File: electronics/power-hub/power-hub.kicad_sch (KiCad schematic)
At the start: 0 parts

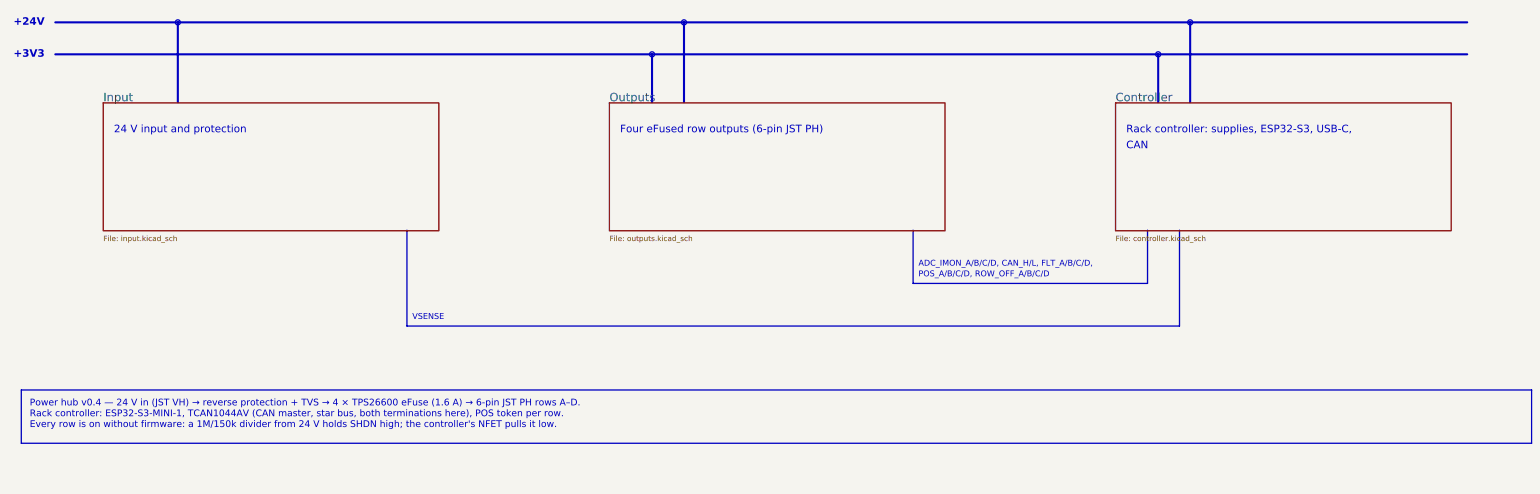
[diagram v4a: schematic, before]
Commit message: Power hub v0.5: USB-C PD input (AP33772S), 4 layers, rows off until enabled
The rack now runs from one USB PD 3.1 charger instead of the GST60A24 brick.

Hub v0.5 (76 x 140 mm, 4 layers, In1 GND, In2 VRACK/+3V3):
* AP33772S sink: 20 V at power-up (VSEL 39k), 28 V EPR on the controller's
  request, never 36/48 V; 5 mOhm Kelvin shunt, back-to-back IRF7842 switch,
  SMAJ30A TVS, NTC by the switch, interrupt and I2C to the ESP32-S3.
* USB4105 5 A receptacle; the controller's buck runs from VBUS (5-28 V),
  ahead of the switch.
* Every row's TPS26600 is off until the controller drives ROW_EN (SHDN pulled
  low); IMON per row; front PD LED.
* ERC 0, DRC 0 errors, 0 unconnected, parity 0; 146 3D models, 0 stand-ins.

Power box: 84 x 148 x 35 mm, hub only (no brick, no cradles), rear USB-C
cut-out, lid on corner lugs.  Viewer, BOM (charger + 5 A e-marked cable,
4-layer JLC estimate) and docs (power, mechanical, cabling, assembly,
electronics) follow.

Co-Authored-By: Claude Opus 5.5 <noreply@anthropic.com>
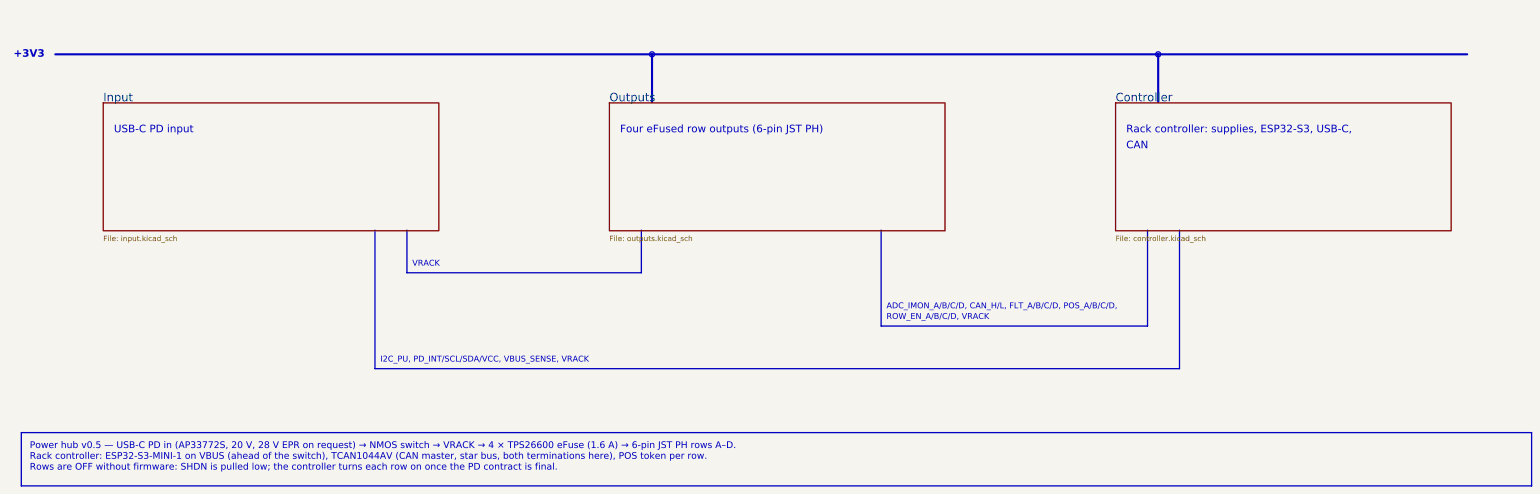
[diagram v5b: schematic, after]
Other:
- note added: "ADC_IMON_A/B/C/D, CAN_H/L, FLT_A/B/C/D, POS_A/B/C/D,"
- note added: "I2C_PU, PD_INT/SCL/SDA/VCC, VBUS_SENSE, VRACK"
- note added: "ROW_EN_A/B/C/D, VRACK"
- note added: "USB-C PD input"
- note added: "VRACK"
- note removed: "+24V"
- note removed: "24 V input and protection"
- note removed: "ADC_IMON_A/B/C/D, CAN_H/L, FLT_A/B/C/D,"
- note removed: "POS_A/B/C/D, ROW_OFF_A/B/C/D"
- note removed: "VSENSE"
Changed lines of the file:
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@@
 	(title_block
 		(title "Power hub — Overview")
-		(rev "0.4")
+		(rev "0.5")
 		(company "hw-testing-rack")
-		(comment 1 "24 V distribution + rack controller (ESP32-S3, CAN master) for the hw-testing-rack")
+		(comment 1 "USB-C PD distribution + rack controller (ESP32-S3, CAN master) for the hw-testing-rack")
 		(comment 2 "Generated from electronics/power-hub/design.py — edit the Python, then regenerate")
 	)
@@
 		)
 	)
-	(text "24 V input and protection"
+	(text "USB-C PD input"
 		(exclude_from_sim no)
 		(at 52.07 77.47 0)
@@
 	(polyline
 		(pts
-			(xy 38.1 50.8)
-			(xy 374.65 50.8)
-		)
-		(stroke
-			(width 0.5)
-			(type default)
-		)
-		(fill
-			(type none)
-		)
-	)
-	(text "+24V"
-		(exclude_from_sim no)
-		(at 35.56 50.8 0)
-		(effects
-			(font
-				(size 1.8 1.8)
-				(bold yes)
-			)
-			(justify right)
-		)
-	)
-	(polyline
-		(pts
-			(xy 67.31 50.8)
-			(xy 67.31 69.85)
-		)
-		(stroke
-			(width 0.5)
-			(type default)
-		)
-		(fill
-			(type none)
-		)
-	)
-	(circle
-		(center 67.31 50.8)
-		(radius 0.6)
-		(stroke
-			(width 0.3)
-			(type default)
-		)
-		(fill
-			(type outline)
-		)
-	)
-	(polyline
-		(pts
-			(xy 187.96 50.8)
-			(xy 187.96 69.85)
-		)
-		(stroke
-			(width 0.5)
-			(type default)
-		)
-		(fill
-			(type none)
-		)
-	)
-	(circle
-		(center 187.96 50.8)
-		(radius 0.6)
-		(stroke
-			(width 0.3)
-			(type default)
-		)
-		(fill
-			(type outline)
-		)
-	)
-	(polyline
-		(pts
-			(xy 308.61 50.8)
-			(xy 308.61 69.85)
-		)
-		(stroke
-			(width 0.5)
-			(type default)
-		)
-		(fill
-			(type none)
-		)
-	)
-	(circle
-		(center 308.61 50.8)
-		(radius 0.6)
-		(stroke
-			(width 0.3)
-			(type default)
-		)
-		(fill
-			(type outline)
-		)
-	)
-	(polyline
-		(pts
-			(xy 242.57 100.33)
-			(xy 242.57 113.03)
-			(xy 298.45 113.03)
+			(xy 121.92 100.33)
+			(xy 121.92 110.49)
+			(xy 177.8 110.49)
+			(xy 177.8 100.33)
+		)
+		(stroke
+			(width 0.3)
+			(type default)
+		)
+		(fill
+			(type none)
+		)
+	)
+	(text "VRACK"
+		(exclude_from_sim no)
+		(at 123.19 109.22 0)
+		(effects
+			(font
+				(size 1.4 1.4)
+			)
+			(justify left bottom)
+		)
+	)
+	(polyline
+		(pts
+			(xy 234.95 100.33)
+			(xy 234.95 123.19)
+			(xy 298.45 123.19)
 			(xy 298.45 100.33)
 		)
@@
 		)
 	)
-	(text "ADC_IMON_A/B/C/D, CAN_H/L, FLT_A/B/C/D,"
-		(exclude_from_sim no)
-		(at 243.84 109.22 0)
+	(text "ADC_IMON_A/B/C/D, CAN_H/L, FLT_A/B/C/D, POS_A/B/C/D,"
+		(exclude_from_sim no)
+		(at 236.22 119.38 0)
 		(effects
 			(font
@@
 		)
 	)
-	(text "POS_A/B/C/D, ROW_OFF_A/B/C/D"
-		(exclude_from_sim no)
-		(at 243.84 111.76 0)
+	(text "ROW_EN_A/B/C/D, VRACK"
+		(exclude_from_sim no)
+		(at 236.22 121.92 0)
 		(effects
 			(font
@@
 	(polyline
 		(pts
-			(xy 121.92 100.33)
-			(xy 121.92 123.19)
-			(xy 306.07 123.19)
+			(xy 114.3 100.33)
+			(xy 114.3 133.35)
+			(xy 306.07 133.35)
 			(xy 306.07 100.33)
 		)
@@
 		)
 	)
-	(text "VSENSE"
-		(exclude_from_sim no)
-		(at 123.19 121.92 0)
+	(text "I2C_PU, PD_INT/SCL/SDA/VCC, VBUS_SENSE, VRACK"
+		(exclude_from_sim no)
+		(at 115.57 132.08 0)
 		(effects
 			(font
@@
 		)
 	)
-	(text_box "Power hub v0.4 — 24 V in (JST VH) → reverse protection + TVS → 4 × TPS26600 eFuse (1.6 A) → 6-pin JST PH rows A–D.\nRack controller: ESP32-S3-MINI-1, TCAN1044AV (CAN master, star bus, both terminations here), POS token per row.\nEvery row is on without firmware: a 1M/150k divider from 24 V holds SHDN high; the controller's NFET pulls it low."
-		(exclude_from_sim no)
-		(at 30 138.43 0)
+	(text_box "Power hub v0.5 — USB-C PD in (AP33772S, 20 V, 28 V EPR on request) → NMOS switch → VRACK → 4 × TPS26600 eFuse (1.6 A) → 6-pin JST PH rows A–D.\nRack controller: ESP32-S3-MINI-1 on VBUS (ahead of the switch), TCAN1044AV (CAN master, star bus, both terminations here), POS token per row.\nRows are OFF without firmware: SHDN is pulled low; the controller turns each row on once the PD contract is final."
+		(exclude_from_sim no)
+		(at 30 148.59 0)
 		(size 360 12.7)
 		(margins 2 2 2 2)

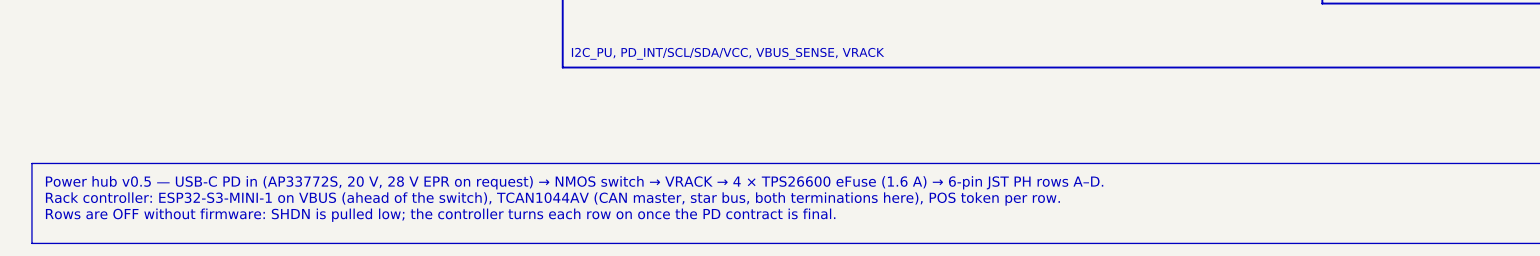
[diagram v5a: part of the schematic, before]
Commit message: CAN transceiver: TCAN1462V (signal improvement) on the hub and the bay node
Same SOIC-8 pinout as the TCAN1044AV (VIO on pin 5, STB on pin 8), so the
footprint, placement and routing are unchanged: the regenerated PCBs keep
every track and via, only U6 / U11's value and fields change.  Signal
improvement (CiA 601-4, ISO 11898-2:2024 set C) damps the ringing of the
star's open branch ends; the termination (56 ohm at the hub) stays.

* catalog: TCAN1462VDRQ1 (C7399456, no LCSC stock on 2026-10-18), with the
  TCAN1044AVDRQ1 (C3234993) and NXP TJA1462AT/0Z (C3234095) as alternates;
  CPL rotation for all three.
* BOM: the board BOMs' alternates now show in the rack BOM notes; JLC
  estimates +$0.54 per board.
* docs/can.md: why the star is fine at 250 kbit/s and what SIC adds, with
  sources (TI SLLSFF2B, SLLA581A; CiA bit-timing table; NXP TJA1462).
* Both boards: ERC 0, DRC 0 errors, 0 unconnected, parity 0; 3D 0 stand-ins.

Co-Authored-By: Claude Opus 5.5 <noreply@anthropic.com>
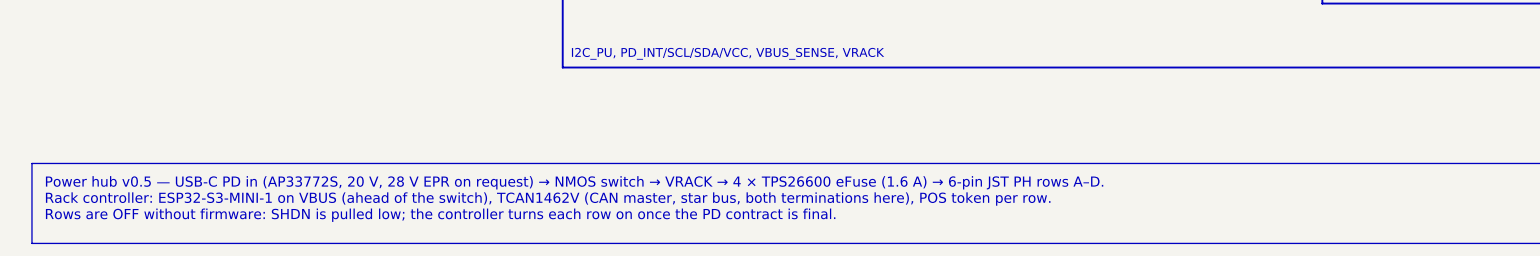
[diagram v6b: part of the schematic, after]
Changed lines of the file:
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@@
 		)
 	)
-	(text_box "Power hub v0.5 — USB-C PD in (AP33772S, 20 V, 28 V EPR on request) → NMOS switch → VRACK → 4 × TPS26600 eFuse (1.6 A) → 6-pin JST PH rows A–D.\nRack controller: ESP32-S3-MINI-1 on VBUS (ahead of the switch), TCAN1044AV (CAN master, star bus, both terminations here), POS token per row.\nRows are OFF without firmware: SHDN is pulled low; the controller turns each row on once the PD contract is final."
+	(text_box "Power hub v0.5 — USB-C PD in (AP33772S, 20 V, 28 V EPR on request) → NMOS switch → VRACK → 4 × TPS26600 eFuse (1.6 A) → 6-pin JST PH rows A–D.\nRack controller: ESP32-S3-MINI-1 on VBUS (ahead of the switch), TCAN1462V (CAN master, star bus, both terminations here), POS token per row.\nRows are OFF without firmware: SHDN is pulled low; the controller turns each row on once the PD contract is final."
 		(exclude_from_sim no)
 		(at 30 148.59 0)

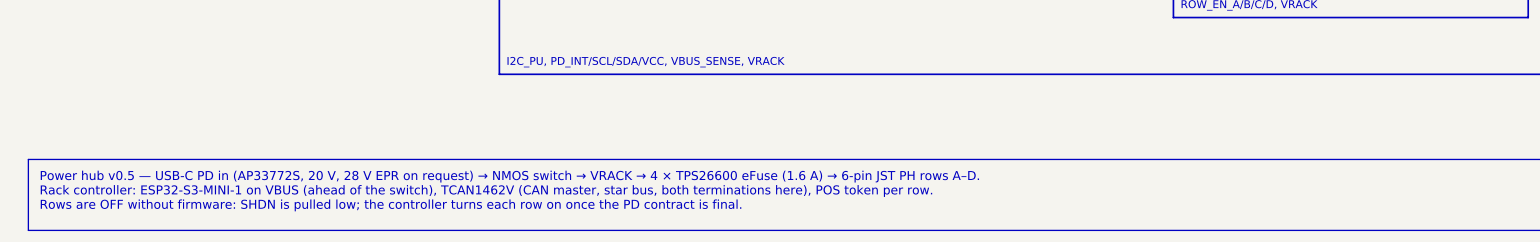
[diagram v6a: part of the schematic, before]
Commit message: Power hub: U1 is the AP33772S FA01 (5 V first), bought through JLC Global Sourcing
The FA02 (VSEL: 20 V by itself) is out of stock everywhere until
≈ 14/12/2026; the user approved the FA01 (2026-10-19): same die, package,
pinout and I2C map, pins 7 and 11 NC.  It takes the charger's 5 V first;
the firmware (7b8a705) sets VSELMIN to 15 V and asks for 20 V / 28 V EPR,
and the rows stay locked out below 15 V.  R7 (an FA02's VSEL resistor)
stays fitted, so an FA02 drops in later.

- catalog: AP33772SDKZ-13-FA01, LCSC C24374260 (0 stock), DigiKey via
  JLC Global Sourcing.
- Hub schematic notes and BOMs regenerated; the routing is the same
  session re-imported (1241 segments, 583 vias, as on main).  ERC 0,
  DRC 0 errors / 0 unconnected / parity 0 (one silk warning, as on main).
- bom.py hub estimate ≈ $227: + $13.30 for 5 parts through Global
  Sourcing (JLC's markup reported ≈ 50 %, no official figure) and
  ≈ 2 weeks for them to reach JLC.
- docs/power.md step 1 and sourcing, electronics.md hub rows,
  bom/sourcing.md: the choice.

Co-Authored-By: Claude Opus 5.5 <noreply@anthropic.com>
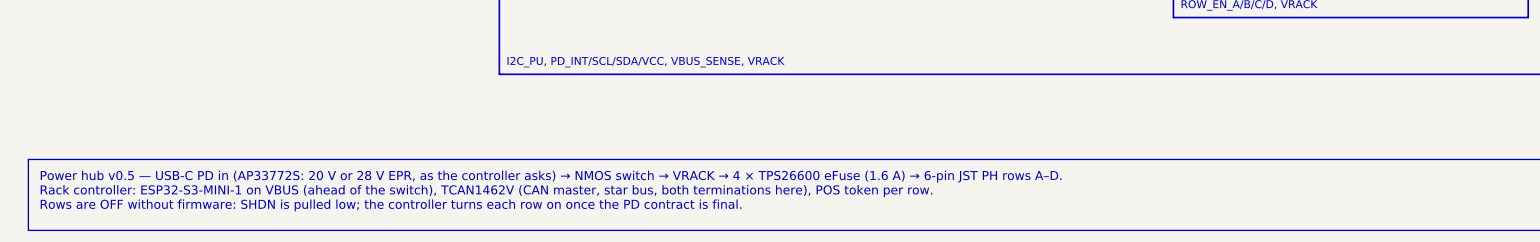
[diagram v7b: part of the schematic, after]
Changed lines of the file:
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@@
 		)
 	)
-	(text_box "Power hub v0.5 — USB-C PD in (AP33772S, 20 V, 28 V EPR on request) → NMOS switch → VRACK → 4 × TPS26600 eFuse (1.6 A) → 6-pin JST PH rows A–D.\nRack controller: ESP32-S3-MINI-1 on VBUS (ahead of the switch), TCAN1462V (CAN master, star bus, both terminations here), POS token per row.\nRows are OFF without firmware: SHDN is pulled low; the controller turns each row on once the PD contract is final."
+	(text_box "Power hub v0.5 — USB-C PD in (AP33772S: 20 V or 28 V EPR, as the controller asks) → NMOS switch → VRACK → 4 × TPS26600 eFuse (1.6 A) → 6-pin JST PH rows A–D.\nRack controller: ESP32-S3-MINI-1 on VBUS (ahead of the switch), TCAN1462V (CAN master, star bus, both terminations here), POS token per row.\nRows are OFF without firmware: SHDN is pulled low; the controller turns each row on once the PD contract is final."
 		(exclude_from_sim no)
 		(at 30 148.59 0)

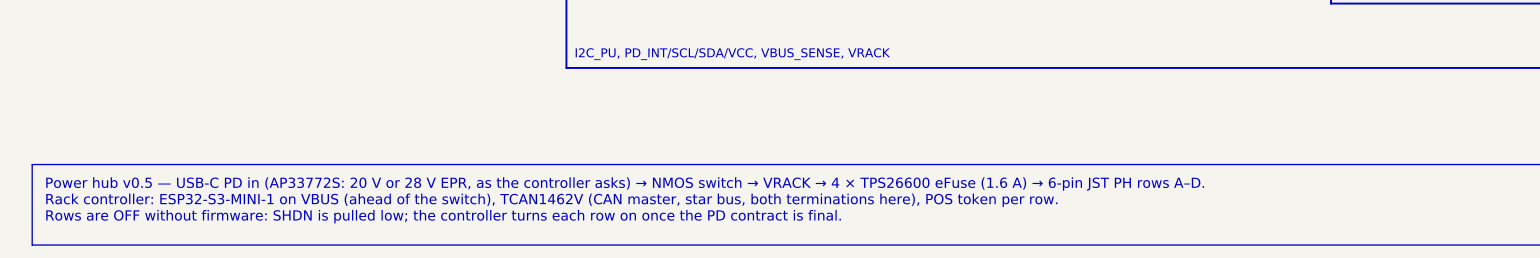
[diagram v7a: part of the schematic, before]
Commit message: CAN transceiver: the TJA1462AT on the hub and the node
The TCAN1462V (C7399456) had no LCSC stock on 2026-10-18 and 19, and
JLC's quote of the hub asked for another part.  The user chose NXP's
TJA1462AT/0Z (C3234095, 10 500 in stock) for both boards (hub U6, node
U11): the same SOIC-8 pinout (VIO on pin 5, STB on pin 8), signal
improvement kept, bus pins -36/+40 V instead of ±58 V.  The TCAN1462V
and the TCAN1044AV stay the alternates.

Both boards regenerated and the same Freerouting sessions re-imported
(tracks and vias unchanged): ERC 0, DRC 0 errors (the hub's known C8
silkscreen warning), 0 unconnected, parity 0, JLC READY.  The CPL keeps
its 270° correction (C3234095 was already in build_board.py).

Docs: can.md, electronics.md, firmware comments and pin tables,
bom/sourcing.md, which also notes that JLC unticks the USB4105 (hard to
process, $0.03 a piece): tick it again at every order.

Co-Authored-By: Claude Opus 5.5 <noreply@anthropic.com>
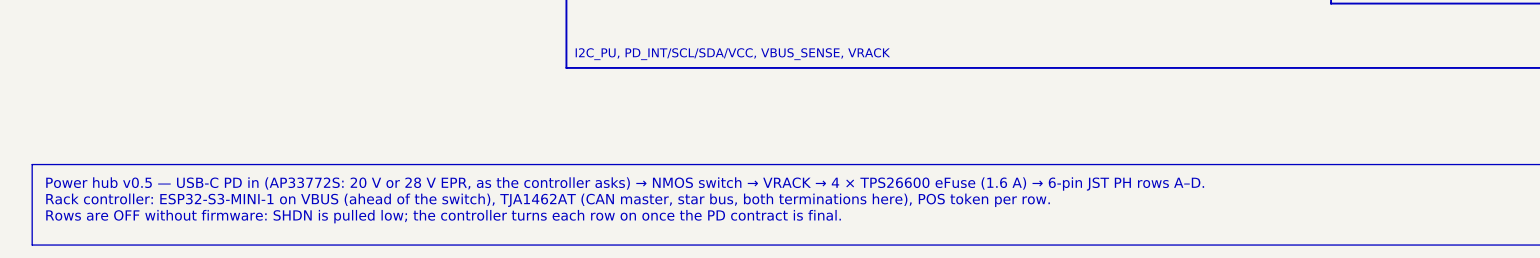
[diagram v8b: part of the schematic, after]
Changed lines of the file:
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@@
 		)
 	)
-	(text_box "Power hub v0.5 — USB-C PD in (AP33772S: 20 V or 28 V EPR, as the controller asks) → NMOS switch → VRACK → 4 × TPS26600 eFuse (1.6 A) → 6-pin JST PH rows A–D.\nRack controller: ESP32-S3-MINI-1 on VBUS (ahead of the switch), TCAN1462V (CAN master, star bus, both terminations here), POS token per row.\nRows are OFF without firmware: SHDN is pulled low; the controller turns each row on once the PD contract is final."
+	(text_box "Power hub v0.5 — USB-C PD in (AP33772S: 20 V or 28 V EPR, as the controller asks) → NMOS switch → VRACK → 4 × TPS26600 eFuse (1.6 A) → 6-pin JST PH rows A–D.\nRack controller: ESP32-S3-MINI-1 on VBUS (ahead of the switch), TJA1462AT (CAN master, star bus, both terminations here), POS token per row.\nRows are OFF without firmware: SHDN is pulled low; the controller turns each row on once the PD contract is final."
 		(exclude_from_sim no)
 		(at 30 148.59 0)
